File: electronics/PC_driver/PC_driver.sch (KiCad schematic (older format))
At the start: 19 parts, among them J1 Conn_Coaxial, J2 Conn_Coaxial, J3 Conn_Coaxial, J4 Jack-DC, SW1 SW_SPDT

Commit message: update board
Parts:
- removed CA1: CA3240, Housings_DIP:DIP-8_W10.16mm, symbol PC_driver-rescue:CA3240
- removed J2: Conn_Coaxial, Connectors:BNC, symbol PC_driver-rescue:Conn_Coaxial
- removed R4: 60, Resistors_THT:R_Axial_DIN0207_L6.3mm_D2.5mm_P10.16mm_Horizontal, symbol PC_driver-rescue:R
- added J?: Conn_Coaxial, Connectors:BNC, symbol PC_driver-rescue:Conn_Coaxial
- added R?: 60, Resistors_THT:R_Axial_DIN0207_L6.3mm_D2.5mm_P10.16mm_Horizontal, symbol PC_driver-rescue:R
- added U?: CA3240AE, PDIP8_LD_INR, symbol ca3240:CA3240AE
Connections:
- net +5V: now also D?.2 (A), U?.4 (V+), U?.5 (VL), U?.8 (V+)
- net D: now also R?.2
- net GND: now also U?.4 (V-)
- net S2: now also U?.1 (OUTPUTA), U?.2 (INV-INPUTA)
- net at SW1.2 (B): now also U?.3 (NON-INV-INPUTA)
- new net: J?.1 (In), U?.6 (INV-INPUTB), U?.7 (OUTPUT)
- new net: R?.1, U?.5 (NON-INV-INPUTB)
- no-connect marks 4 -> 2
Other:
- moved on the sheet: J3, J4, R?, U?A

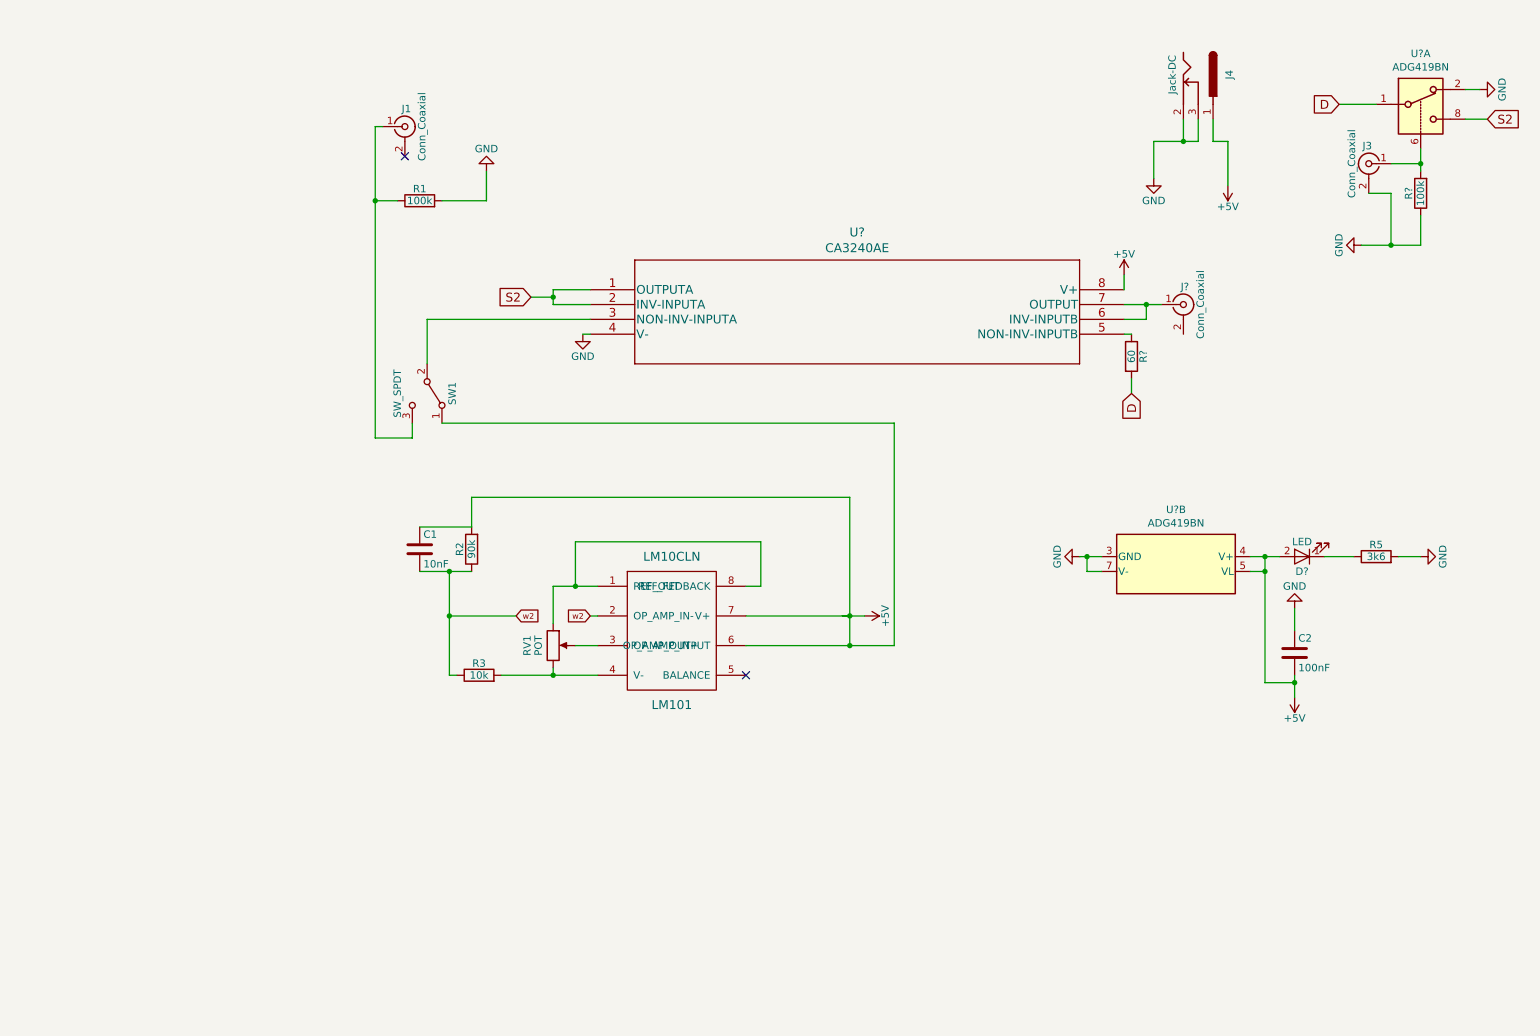
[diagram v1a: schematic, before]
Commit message: fix labels and buggy resistor
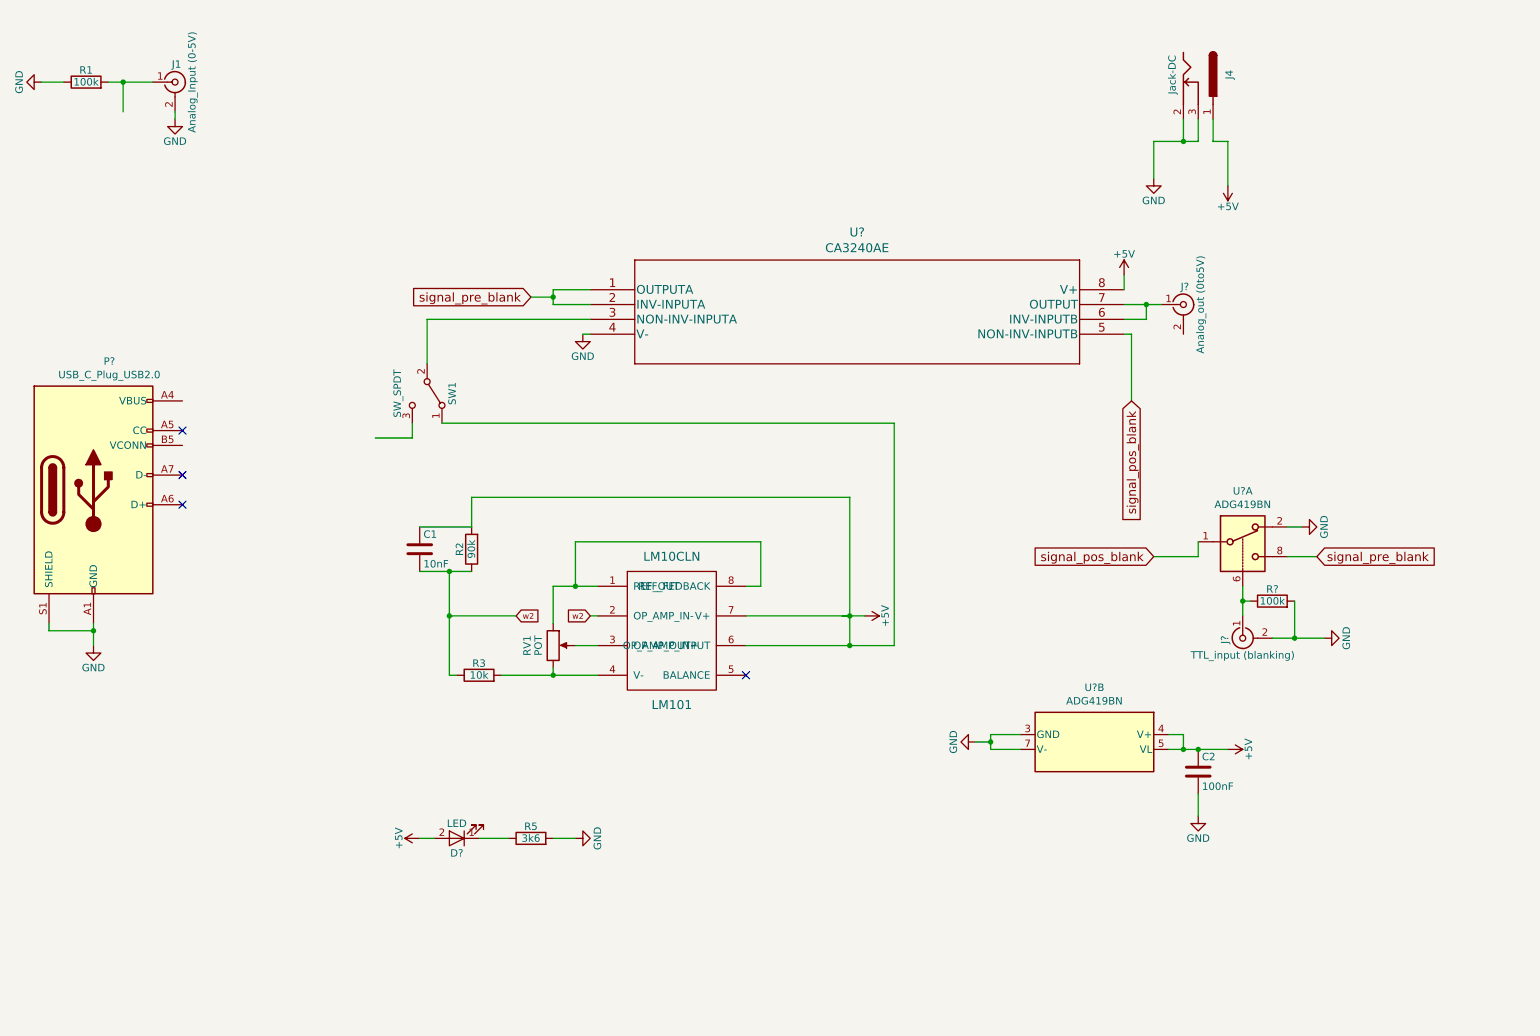
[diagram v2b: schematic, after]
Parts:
- removed J3: Conn_Coaxial, Connectors:BNC, symbol PC_driver-rescue:Conn_Coaxial
- removed R?: 100k, Resistors_THT:R_Axial_DIN0207_L6.3mm_D2.5mm_P10.16mm_Horizontal, symbol PC_driver-rescue:R
- removed R?: 60, Resistors_THT:R_Axial_DIN0207_L6.3mm_D2.5mm_P10.16mm_Horizontal, symbol PC_driver-rescue:R
- removed U? (x2): ADG419BN, Package_DIP:DIP-8_W7.62mm, symbol Analog_Switch:ADG419BN
- added J?: TTL_input (blanking), Connectors:BNC, symbol PC_driver-rescue:Conn_Coaxial
- added P?: USB_C_Plug_USB2.0, symbol Connector:USB_C_Plug_USB2.0
- added R?: 100k, Resistors_THT:R_Axial_DIN0207_L6.3mm_D2.5mm_P10.16mm_Horizontal, symbol PC_driver-rescue:R
- added U? (x2): ADG419BN, Package_DIP:DIP-8_W7.62mm, symbol Analog_Switch:ADG419BN
- J1: value Conn_Coaxial -> Analog_Input (0-5V)
- J?: value Conn_Coaxial -> Analog_out (0to5V)
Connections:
- net labels added: signal_pos_blank, signal_pre_blank
- net labels removed: D, S2
- wire segments 87 -> 88
- no-connect marks 2 -> 4
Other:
- moved on the sheet: C2, D?, J1, R1, R5

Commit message: finished schmatics and footprint association
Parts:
- removed J4: Jack-DC, Connectors:BARREL_JACK, symbol PC_driver-rescue:Jack-DC
- removed LM101: LM10CLN, Housings_DIP:DIP-8_W10.16mm, symbol PC_driver-rescue:LM10CLN
- added C3: 100nF, Capacitor_THT:C_Disc_D5.0mm_W2.5mm_P2.50mm, symbol PC_driver-rescue:C
- added D2: switch_led, LED_THT:LED_D5.0mm_Clear, symbol PC_driver-rescue:LED
- added J2: add_resist_jumper, Connector_PinHeader_2.54mm:PinHeader_1x03_P2.54mm_Vertical, symbol Connector:Conn_01x03_Male
- added R4: 60, Resistor_THT:R_Axial_DIN0309_L9.0mm_D3.2mm_P12.70mm_Horizontal, symbol PC_driver-rescue:R
- added R7: 3k6, Resistor_THT:R_Axial_DIN0309_L9.0mm_D3.2mm_P15.24mm_Horizontal, symbol PC_driver-rescue:R
- added U1: LM10CLN, Package_DIP:DIP-8_W7.62mm, symbol lm10cln:LM10CLN
- C1: footprint Capacitors_THT:C_Rect_L10.3mm_W4.5mm_P7.50mm_MKS4 -> Capacitor_THT:C_Disc_D5.0mm_W2.5mm_P2.50mm
- C2: footprint Capacitors_THT:C_Rect_L13.0mm_W4.0mm_P10.00mm_FKS3_FKP3_MKS4 -> Capacitor_THT:C_Disc_D5.0mm_W2.5mm_P2.50mm
- D1: renamed from D?; value LED -> potent_led; footprint LEDs:LED_PLCC-2 -> LED_THT:LED_D5.0mm_Clear
- J1: footprint Connectors:BNC -> Connector_Coaxial:BNC_Amphenol_B6252HB-NPP3G-50_Horizontal
- J3, J4: renamed from J?; footprint Connectors:BNC -> Connector_Coaxial:BNC_Amphenol_B6252HB-NPP3G-50_Horizontal
- P1: renamed from P?; footprint (none) -> Connector_USB:USB_C_Receptacle_GCT_USB4085
- R1, R2, R3, R5: footprint Resistors_THT:R_Axial_DIN0207_L6.3mm_D2.5mm_P10.16mm_Horizontal -> Resistor_THT:R_Axial_DIN0309_L9.0mm_D3.2mm_P12.70mm_Horizontal
- R6: renamed from R?; footprint Resistors_THT:R_Axial_DIN0207_L6.3mm_D2.5mm_P10.16mm_Horizontal -> Resistor_THT:R_Axial_DIN0309_L9.0mm_D3.2mm_P12.70mm_Horizontal
- RV1: value POT -> laser_int 5k; footprint Potentiometers:Potentiometer_WirePads -> Potentiometer_THT:Potentiometer_ACP_CA14-H5_Horizontal
- SW1: footprint Buttons_Switches_SMD:SW_SPDT_CK-JS102011SAQN -> Button_Switch_THT:SW_E-Switch_EG1224_SPDT_Angled
- U2: renamed from U?; footprint PDIP8_LD_INR -> Package_DIP:DIP-8_W7.62mm
- gave numbers to parts that had none: 1
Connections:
- net labels added: analog_input, internal_signal, pin2, pin7to2
- net labels removed: w2
- wire segments 88 -> 105
- no-connect marks 4 -> 3
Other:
- moved on the sheet: C2, D1, R5, U3B

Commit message: finish part placement, wiring and plotting
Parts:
- R7: footprint Resistor_THT:R_Axial_DIN0309_L9.0mm_D3.2mm_P15.24mm_Horizontal -> Resistor_THT:R_Axial_DIN0309_L9.0mm_D3.2mm_P12.70mm_Horizontal
- renumbered C3 to C1, C1 to C2, C2 to C3, R3 to R2, R5 to R3, R2 to R5
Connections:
- net +5V: no longer C2.2, R5.1, SW1.1 (A), U1.6 (OUT)
- net GND: now also J3.2 (Ext)
- new net internal_signal: C2.2, R5.1, SW1.1 (A), U1.6 (OUT)
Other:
- moved on the sheet: C2, R5
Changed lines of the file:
@@
 $EndComp
 $Comp
-L power:GND #PWR03
+L power:GND #PWR01
 U 1 1 5E147AB2
 P 1300 950
-F 0 "#PWR03" H 1300 700 50  0001 C CNN
+F 0 "#PWR01" H 1300 700 50  0001 C CNN
 F 1 "GND" H 1300 800 50  0000 C CNN
 F 2 "" H 1300 950 50  0001 C CNN
@@
 $EndComp
 $Comp
-L PC_driver-rescue:R R5
+L PC_driver-rescue:R R3
 U 1 1 5E64ED6F
 P 3250 7150
-F 0 "R5" V 3330 7150 50  0000 C CNN
+F 0 "R3" V 3330 7150 50  0000 C CNN
 F 1 "3k6" V 3250 7150 50  0000 C CNN
 F 2 "Resistor_THT:R_Axial_DIN0309_L9.0mm_D3.2mm_P12.70mm_Horizontal" V 3180 7150 50  0001 C CNN
@@
 	3400 7150 3550 7150
 $Comp
-L PC_driver-rescue:C C2
+L PC_driver-rescue:C C3
 U 1 1 5E65749E
 P 10450 5600
-F 0 "C2" H 10475 5700 50  0000 L CNN
+F 0 "C3" H 10475 5700 50  0000 L CNN
 F 1 "100nF" H 10475 5500 50  0000 L CNN
 F 2 "Capacitor_THT:C_Disc_D5.0mm_W2.5mm_P2.50mm" H 10488 5450 50  0001 C CNN
@@
 $EndComp
 $Comp
-L power:GND #PWR016
+L power:GND #PWR018
 U 1 1 5E662838
 P 10450 5900
-F 0 "#PWR016" H 10450 5650 50  0001 C CNN
+F 0 "#PWR018" H 10450 5650 50  0001 C CNN
 F 1 "GND" H 10450 5750 50  0000 C CNN
 F 2 "" H 10450 5900 50  0001 C CNN
@@
 	3900 2550 3900 2850
 $Comp
-L power:+5V #PWR012
+L power:+5V #PWR013
 U 1 1 5EDF798C
 P 8600 2250
-F 0 "#PWR012" H 8600 2100 50  0001 C CNN
+F 0 "#PWR013" H 8600 2100 50  0001 C CNN
 F 1 "+5V" H 8600 2390 50  0000 C CNN
 F 2 "" H 8600 2250 50  0001 C CNN
@@
 	2500 7150 2600 7150
 $Comp
-L power:GND #PWR02
+L power:GND #PWR03
 U 1 1 5ED69F36
 P 2200 1200
-F 0 "#PWR02" H 2200 950 50  0001 C CNN
+F 0 "#PWR03" H 2200 950 50  0001 C CNN
 F 1 "GND" H 2200 1050 50  0000 C CNN
 F 2 "" H 2200 1200 50  0001 C CNN
@@
 $EndComp
 $Comp
-L power:GND #PWR015
+L power:GND #PWR017
 U 1 1 5ED83FE0
 P 9950 4700
-F 0 "#PWR015" H 9950 4450 50  0001 C CNN
+F 0 "#PWR017" H 9950 4450 50  0001 C CNN
 F 1 "GND" H 9950 4550 50  0000 C CNN
 F 2 "" H 9950 4700 50  0001 C CNN
@@
 	10350 5450 10250 5450
 $Comp
-L power:GND #PWR013
+L power:GND #PWR014
 U 1 1 5EDD9AEE
 P 8950 5400
-F 0 "#PWR013" H 8950 5150 50  0001 C CNN
+F 0 "#PWR014" H 8950 5150 50  0001 C CNN
 F 1 "GND" H 8950 5250 50  0000 C CNN
 F 2 "" H 8950 5400 50  0001 C CNN
@@
 	9100 4150 9100 4050
 $Comp
-L power:GND #PWR014
+L power:GND #PWR016
 U 1 1 5EE2185F
 P 9800 3950
-F 0 "#PWR014" H 9800 3700 50  0001 C CNN
+F 0 "#PWR016" H 9800 3700 50  0001 C CNN
 F 1 "GND" H 9800 3800 50  0000 C CNN
 F 2 "" H 9800 3950 50  0001 C CNN
@@
 $EndComp
 $Comp
-L power:GND #PWR01
+L power:GND #PWR02
 U 1 1 5EE3ABB2
 P 1650 4750
-F 0 "#PWR01" H 1650 4500 50  0001 C CNN
+F 0 "#PWR02" H 1650 4500 50  0001 C CNN
 F 1 "GND" H 1650 4600 50  0000 C CNN
 F 2 "" H 1650 4750 50  0001 C CNN
@@
 Text GLabel 3550 3350 0    50   Input ~ 0
 analog_input
-Text GLabel 4250 3250 2    50   Input ~ 0
-internal_signal
-Wire Wire Line
-	4000 3250 4250 3250
 $Comp
 L PC_driver-rescue:POT RV1
@@
 Connection ~ 3050 5750
 $Comp
-L PC_driver-rescue:C C3
+L PC_driver-rescue:C C1
 U 1 1 5EE70AB2
 P 7350 5650
-F 0 "C3" H 7375 5750 50  0000 L CNN
+F 0 "C1" H 7375 5750 50  0000 L CNN
 F 1 "100nF" H 7375 5550 50  0000 L CNN
 F 2 "Capacitor_THT:C_Disc_D5.0mm_W2.5mm_P2.50mm" H 7388 5500 50  0001 C CNN
@@
 	1    0    0    -1
 $EndComp
-Text GLabel 7900 5950 2    50   Input ~ 0
-internal_signal
 Wire Wire Line
 	7200 5850 7350 5850
@@
 Connection ~ 7350 5850
 $Comp
-L power:GND #PWR010
+L power:GND #PWR011
 U 1 1 5EE7F0DA
 P 7350 5350
-F 0 "#PWR010" H 7350 5100 50  0001 C CNN
+F 0 "#PWR011" H 7350 5100 50  0001 C CNN
 F 1 "GND" H 7350 5200 50  0000 C CNN
 F 2 "" H 7350 5350 50  0001 C CNN
@@
 Connection ~ 3050 6300
 $Comp
-L PC_driver-rescue:R R3
+L PC_driver-rescue:R R2
 U 1 1 5EE981C9
 P 2550 5950
-F 0 "R3" V 2630 5950 50  0000 C CNN
+F 0 "R2" V 2630 5950 50  0000 C CNN
 F 1 "10k" V 2550 5950 50  0000 C CNN
 F 2 "Resistor_THT:R_Axial_DIN0309_L9.0mm_D3.2mm_P12.70mm_Horizontal" V 2480 5950 50  0001 C CNN
@@
 	1    0    0    -1
 $EndComp
-$Comp
-L PC_driver-rescue:R R2
-U 1 1 5EEAAB15
-P 2050 5900
-F 0 "R2" V 2130 5900 50  0000 C CNN
-F 1 "90k" V 2050 5900 50  0000 C CNN
-F 2 "Resistor_THT:R_Axial_DIN0309_L9.0mm_D3.2mm_P12.70mm_Horizontal" V 1980 5900 50  0001 C CNN
-F 3 "" H 2050 5900 50  0001 C CNN
-	1    2050 5900
-	0    -1   -1   0
-$EndComp
-Wire Wire Line
-	2250 5900 2200 5900
-$Comp
-L PC_driver-rescue:C C1
-U 1 1 5EEAECED
-P 2050 5650
-F 0 "C1" H 2075 5750 50  0000 L CNN
-F 1 "10nF" H 2075 5550 50  0000 L CNN
-F 2 "Capacitor_THT:C_Disc_D5.0mm_W2.5mm_P2.50mm" H 2088 5500 50  0001 C CNN
-F 3 "" H 2050 5650 50  0001 C CNN
-	1    2050 5650
-	0    1    1    0
-$EndComp
-Wire Wire Line
-	2250 5650 2200 5650
-Wire Wire Line
-	1900 5900 1800 5900
-Wire Wire Line
-	1800 5900 1800 5750
-Wire Wire Line
-	1800 5650 1900 5650
-$Comp
-L power:+5V #PWR011
-U 1 1 5EE7BC4C
-P 7700 5700
-F 0 "#PWR011" H 7700 5550 50  0001 C CNN
-F 1 "+5V" H 7700 5840 50  0000 C CNN
-F 2 "" H 7700 5700 50  0001 C CNN
-F 3 "" H 7700 5700 50  0001 C CNN
-	1    7700 5700
-	1    0    0    -1
-$EndComp
-Wire Wire Line
-	7700 5850 7700 5700
-Wire Wire Line
-	7200 5950 7800 5950
-Wire Wire Line
-	7350 5850 7550 5850
-Wire Wire Line
-	7700 5850 7800 5850
-Wire Wire Line
-	7800 5850 7800 5950
-Connection ~ 7700 5850
-Connection ~ 7800 5950
-Wire Wire Line
-	7800 5950 7900 5950
-Text GLabel 1650 5750 0    50   Input ~ 0
-pin7to2
-Wire Wire Line
-	1650 5750 1800 5750
-Connection ~ 1800 5750
-Wire Wire Line
-	1800 5750 1800 5650
-Text GLabel 7550 5750 1    50   Input ~ 0
-pin7to2
-Wire Wire Line
-	7550 5750 7550 5850
-Connection ~ 7550 5850
-Wire Wire Line
-	7550 5850 7700 5850
-Wire Wire Line
-	2550 5700 2550 5750
-Wire Wire Line
-	2250 5750 2550 5750
-Wire Wire Line
-	2250 5650 2250 5750
-Connection ~ 2250 5750
-Wire Wire Line
-	2250 5750 2250 5900
-Connection ~ 2550 5750
-Wire Wire Line
-	2550 5750 2550 5800
 $Comp
 L power:+5V #PWR05
@@
 	0    1    1    0
 $EndComp
-Wire Wire Line
-	2400 3100 2250 3100
 $Comp
 L power:GND #PWR04
@@
 F 0 "R7" V 11030 6000 50  0000 C CNN
 F 1 "3k6" V 10950 6000 50  0000 C CNN
-F 2 "Resistor_THT:R_Axial_DIN0309_L9.0mm_D3.2mm_P15.24mm_Horizontal" V 10880 6000 50  0001 C CNN
+F 2 "Resistor_THT:R_Axial_DIN0309_L9.0mm_D3.2mm_P12.70mm_Horizontal" V 10880 6000 50  0001 C CNN
 F 3 "" H 10950 6000 50  0001 C CNN
 	1    10950 6000
@@
 $EndComp
 $Comp
-L power:GND #PWR018
+L power:GND #PWR020
 U 1 1 5EF0F7AE
 P 10950 6300
-F 0 "#PWR018" H 10950 6050 50  0001 C CNN
+F 0 "#PWR020" H 10950 6050 50  0001 C CNN
 F 1 "GND" H 10950 6150 50  0000 C CNN
 F 2 "" H 10950 6300 50  0001 C CNN
@@
 	10950 6150 10950 6300
 $Comp
-L power:+5V #PWR017
+L power:+5V #PWR019
 U 1 1 5EF0F7B6
 P 10950 5250
-F 0 "#PWR017" H 10950 5100 50  0001 C CNN
+F 0 "#PWR019" H 10950 5100 50  0001 C CNN
 F 1 "+5V" H 10950 5390 50  0000 C CNN
 F 2 "" H 10950 5250 50  0001 C CNN
@@
 	8650 2650 8650 3350
 $Comp
-L power:GND #PWR019
+L power:GND #PWR010
 U 1 1 5EF75A5B
 P 7300 6100
-F 0 "#PWR019" H 7300 5850 50  0001 C CNN
+F 0 "#PWR010" H 7300 5850 50  0001 C CNN
 F 1 "GND" H 7300 5950 50  0000 C CNN
 F 2 "" H 7300 6100 50  0001 C CNN
@@
 Wire Wire Line
 	7300 6050 7200 6050
+$Comp
+L power:GND #PWR015
+U 1 1 5ED7B843
+P 9000 2750
+F 0 "#PWR015" H 9000 2500 50  0001 C CNN
+F 1 "GND" H 9000 2600 50  0000 C CNN
+F 2 "" H 9000 2750 50  0001 C CNN
+F 3 "" H 9000 2750 50  0001 C CNN
+	1    9000 2750
+	1    0    0    -1
+$EndComp
+Wire Wire Line
+	9000 2650 9000 2750
+Wire Wire Line
+	7350 5850 7550 5850
+Wire Wire Line
+	7200 5950 7800 5950
+$Comp
+L PC_driver-rescue:R R5
+U 1 1 5EEAAB15
+P 8300 6200
+F 0 "R5" V 8380 6200 50  0000 C CNN
+F 1 "90k" V 8300 6200 50  0000 C CNN
+F 2 "Resistor_THT:R_Axial_DIN0309_L9.0mm_D3.2mm_P12.70mm_Horizontal" V 8230 6200 50  0001 C CNN
+F 3 "" H 8300 6200 50  0001 C CNN
+	1    8300 6200
+	0    -1   -1   0
+$EndComp
+Wire Wire Line
+	8500 6200 8450 6200
+$Comp
+L PC_driver-rescue:C C2
+U 1 1 5EEAECED
+P 8300 5950
+F 0 "C2" H 8325 6050 50  0000 L CNN
+F 1 "10nF" H 8325 5850 50  0000 L CNN
+F 2 "Capacitor_THT:C_Disc_D5.0mm_W2.5mm_P2.50mm" H 8338 5800 50  0001 C CNN
+F 3 "" H 8300 5950 50  0001 C CNN
+	1    8300 5950
+	0    1    1    0
+$EndComp
+Wire Wire Line
+	8500 5950 8450 5950
+Wire Wire Line
+	8150 6200 8050 6200
+Wire Wire Line
+	8050 6200 8050 6050
+Wire Wire Line
+	8050 5950 8150 5950
+Wire Wire Line
+	7900 6050 8050 6050
+Connection ~ 8050 6050
+Wire Wire Line
+	8050 6050 8050 5950
+Wire Wire Line
+	7900 6050 7900 5950
+Wire Wire Line
+	2550 5700 2550 5800
+Text GLabel 8600 6050 1    50   Input ~ 0
+pin2
+Wire Wire Line
+	8500 5950 8500 6050
+Wire Wire Line
+	8600 6050 8500 6050
+Connection ~ 8500 6050
+Wire Wire Line
+	8500 6050 8500 6200
+Text GLabel 4000 3400 2    50   Input ~ 0
+internal_signal
+Wire Wire Line
+	4000 3250 4000 3400
+Text GLabel 7800 5750 1    50   Input ~ 0
+internal_signal
+Wire Wire Line
+	7800 5750 7800 5950
+Connection ~ 7800 5950
+Wire Wire Line
+	7800 5950 7900 5950
+Wire Wire Line
+	2250 3100 2400 3100
+$Comp
+L power:+5V #PWR012
+U 1 1 5EDEFA0E
+P 7550 5850
+F 0 "#PWR012" H 7550 5700 50  0001 C CNN
+F 1 "+5V" H 7550 5990 50  0000 C CNN
+F 2 "" H 7550 5850 50  0001 C CNN
+F 3 "" H 7550 5850 50  0001 C CNN
+	1    7550 5850
+	0    1    1    0
+$EndComp
 $EndSCHEMATC
